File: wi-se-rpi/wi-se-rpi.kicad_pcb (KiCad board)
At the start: 4 copper layers, 29.2 x 19.5 mm, 43 parts, among them J1 RASPI, SW1 RESET, SW2 BOOT0, SW3 FLASH_EN_SW, U1 AMS1117-3.3, U2 ESP-WROOM-02, U3 MC74VHC1G, U4 NL27WZ00, U5 NL27WZ32

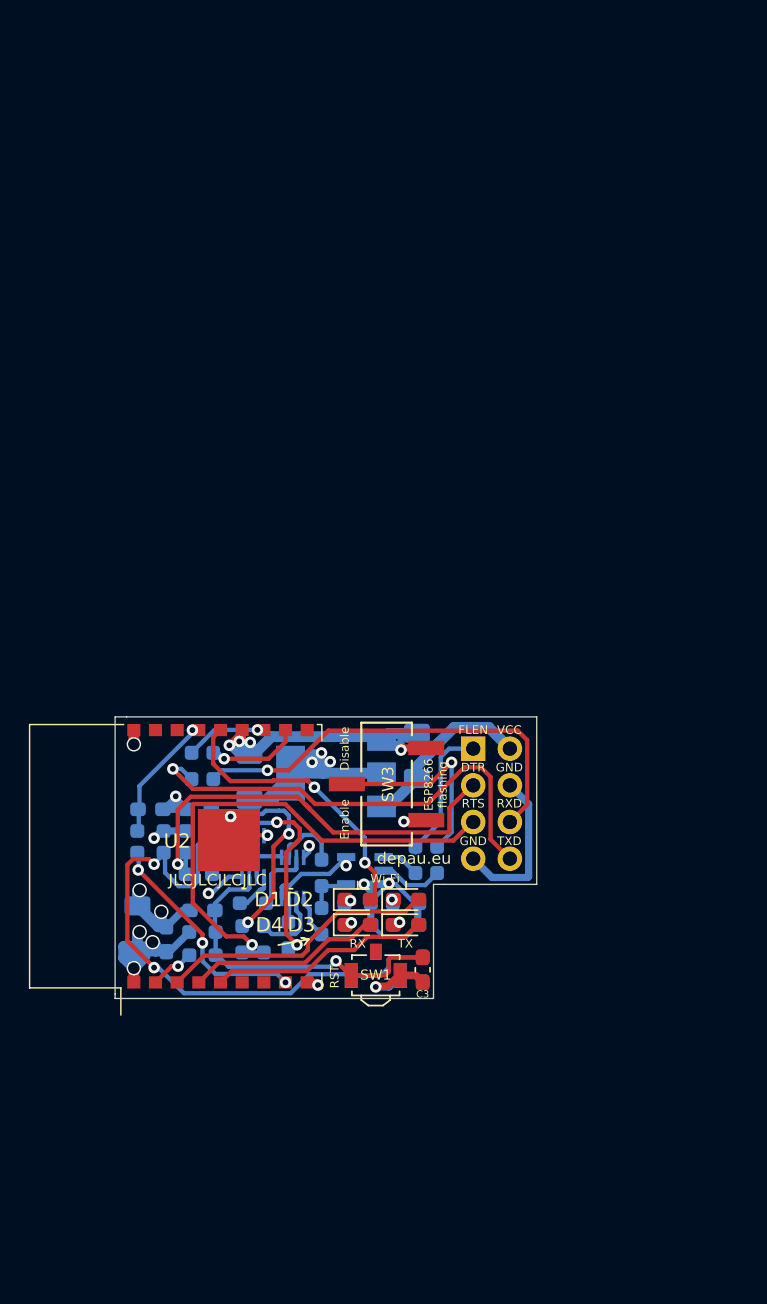
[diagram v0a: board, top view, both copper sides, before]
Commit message: Make RPI version as small as it can be
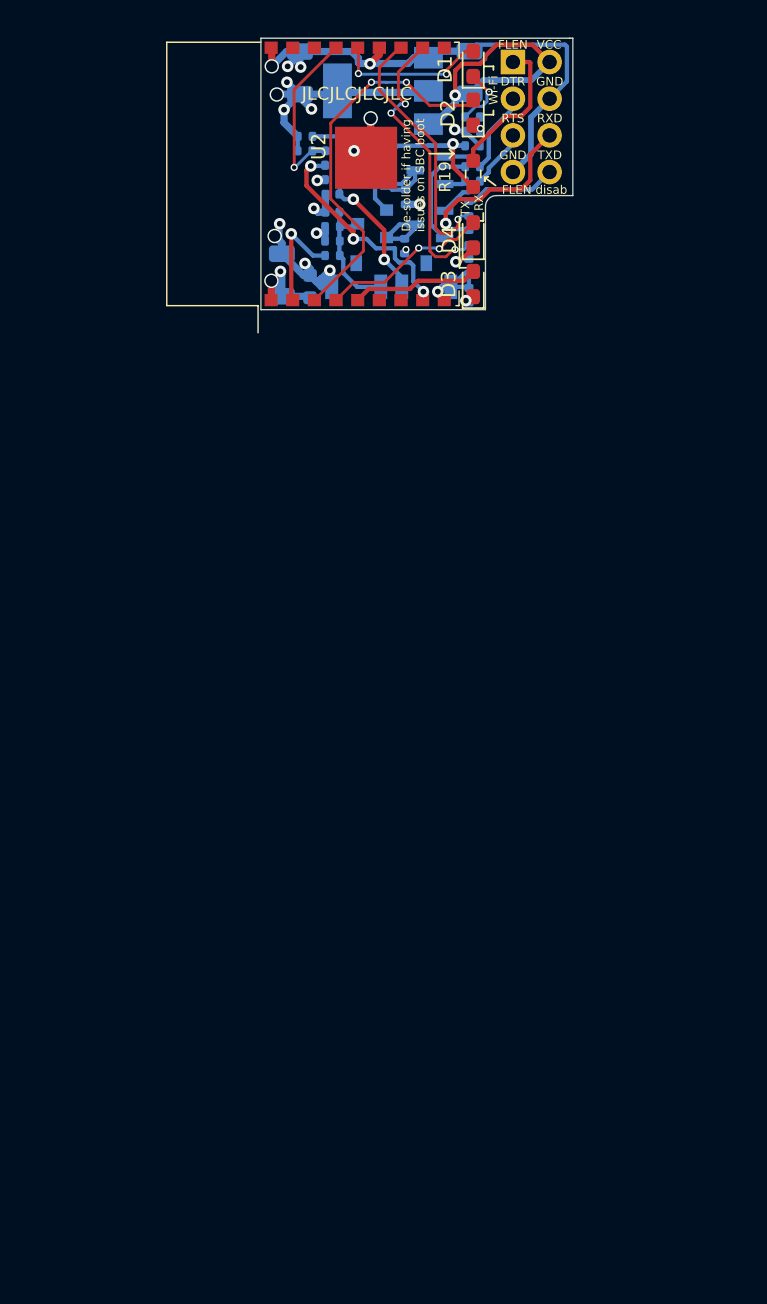
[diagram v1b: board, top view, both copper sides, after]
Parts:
- removed C3, C4: 0u1, Capacitor_SMD:C_0603_1608Metric_Pad1.08x0.95mm_HandSolder
- removed R20, R21: 10k, Resistor_SMD:R_0603_1608Metric_Pad0.98x0.95mm_HandSolder
- removed SW3: FLASH_EN_SW, JS102011SCQN:CK-JS102011SCQN-0-0-0
- removed U3: MC74VHC1G, ON-gates:SOT95P280X145-5N
- removed U4: NL27WZ00, ON-gates:SOP50P310X90-8N
- removed U5: NL27WZ32, ON-gates:SOP50P310X90-8N
- added Q1: SS8050-G, SS8050-G:SS8050-G, B.Cu at (85.0, 9.50)
- added Q2: SS8050-G, SS8050-G:SS8050-G, B.Cu at (85.0, 5.75)
- added Q3: 2N7002, Package_TO_SOT_SMD:SOT-23, B.Cu at (81.0, 9.45)
- added Q4: 2N7002, Package_TO_SOT_SMD:SOT-23, B.Cu at (81.0, 5.75)
- C1, C2, C5: footprint Capacitor_SMD:C_1206_3216Metric_Pad1.33x1.80mm_HandSolder -> Capacitor_SMD:C_1206_3216Metric
- C6: footprint Capacitor_SMD:C_0603_1608Metric_Pad1.08x0.95mm_HandSolder -> Capacitor_SMD:C_0603_1608Metric
- C7, C8, C9: footprint Capacitor_SMD:C_0603_1608Metric_Pad1.08x0.95mm_HandSolder -> Capacitor_SMD:C_0402_1005Metric
- R1, R14, R15, R16, R17, R18, R2, R3, R4, R5, R6, R7, R8, R9: footprint Resistor_SMD:R_0603_1608Metric_Pad0.98x0.95mm_HandSolder -> Resistor_SMD:R_0402_1005Metric
- R10, R11, R12, R13: value 0 -> 1k; footprint Resistor_SMD:R_0603_1608Metric_Pad0.98x0.95mm_HandSolder -> Resistor_SMD:R_0402_1005Metric
- R19: value 10k -> 0; moved to F.Cu
- SW1: footprint Button_Switch_SMD:SW_SPST_B3U-3100P -> wi-se:SW_SPST_B3U-3100P_silk_change; moved to B.Cu
- SW2: footprint Button_Switch_SMD:SW_SPST_B3U-3100P -> wi-se:SW_SPST_B3U-3100P_silk_change
- moved D1 58.4 mm to (88.0, -1.62), turned to 90 degrees
- moved R18 57.2 mm to (88.0, 4.05), turned to 180 degrees
- moved R1 55.0 mm to (88.0, 2.05)
- moved D2 54.7 mm to (88.0, 1.75), turned to 90 degrees
- moved R19 54.2 mm to (88.0, 6.00), turned to 270 degrees
- moved R2 53.6 mm to (88.0, 3.05), turned to 0 degrees
- moved R17 52.8 mm to (78.2, 6.40), turned to 180 degrees
- moved R10 49.3 mm to (78.2, 11.7)
- moved R13 49.2 mm to (78.2, 5.40)
- moved C8 49.2 mm to (78.2, 8.65)
- moved C2 48.9 mm to (76.0, -1.00)
- moved R6 48.7 mm to (78.2, 10.7)
- moved R5 48.7 mm to (76.4, 3.40)
- moved D4 48.4 mm to (88.0, 10.2), turned to 90 degrees
- moved R7 48.3 mm to (76.3, 4.40), turned to 0 degrees
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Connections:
- J1 pad 1: FLASH_EN -> Net-(J1-Pad1)
- R14 pad 2: DTR -> +3V3
- R15 pad 2: Net-(R15-Pad2) -> +3V3
- R16 pad 1: Net-(R16-Pad1) -> EN
- R16 pad 2: Net-(R15-Pad2) -> +3V3
- R17 pad 1: Net-(R17-Pad1) -> BOOT0
- R17 pad 2: RTS -> +3V3
- R18 pad 1: Net-(R18-Pad1) -> GND
- R18 pad 2: RTS -> FLASH_EN
- R19 pad 1: Net-(R19-Pad1) -> Net-(J1-Pad1)
- R19 pad 2: Net-(R19-Pad2) -> FLASH_EN
- R8 pad 2: FLASH_EN -> DTR
- R9 pad 1: Net-(R9-Pad1) -> RTS
- R9 pad 2: FLASH_EN_SW -> Net-(Q2-Pad2)
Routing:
- net RTS: track 35.1 -> 7.41 mm, vias 1 -> 0
- net BOOT0: track 45.9 -> 18.7 mm
- net TXD: track 32.1 -> 6.43 mm, vias 1 -> 0
- net DTR: track 30.6 -> 8.39 mm, vias 1 -> 0
- net +3V3: track 48.4 -> 28.3 mm
- net RXD: track 29.8 -> 13.4 mm
- net Net-(R19-Pad1): track 14.8 -> 0.00 mm, vias 2 -> 0
- net EN: track 23.4 -> 8.64 mm, vias 1 -> 0
- net Net-(R18-Pad1): track 14.5 -> 0.00 mm, vias 2 -> 0
- net FLASH_EN_SW: track 14.1 -> 0.00 mm, vias 1 -> 0
- net Net-(R11-Pad1): track 6.47 -> 19.9 mm, vias 1 -> 3
- net Net-(R12-Pad1): track 5.66 -> 18.2 mm
- net Net-(J1-Pad1): track 0.00 -> 10.3 mm
- net GND: track 77.9 -> 68.3 mm, vias 15 -> 13
- net LED_WIFI: track 19.9 -> 10.5 mm
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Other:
- board size 29.2 x 19.5 mm -> 21.6 x 18.8 mm
- rule via_min_drill: 0.3 -> 0.2
- rule via_min_size: 0.4 -> 0.45
- board text added: "De-solder if having issues on SBC boot"
- board text added: "FLEN disab"
- board text added: "IO0"
- board text added: "v0.1 for rpi"
- board text removed: "BOOT0"
- board text removed: "Disable"
- board text removed: "ESP8266 flashing"
- board text removed: "Enable"
- board text removed: "v0.1 for *pi"

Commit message: Final version of rpi variant (last famous words)
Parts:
- moved SW1 0.76 mm to (80.0, 13.8)
- moved SW2 0.72 mm to (84.8, 13.7)
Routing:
- net EN: track 8.64 -> 9.43 mm
- net Net-(D3-Pad1): track 0.89 -> 1.46 mm
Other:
- board size 21.6 x 18.8 mm -> 21.6 x 20 mm

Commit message: Ground switch shields
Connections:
- SW1 pad 3: (no net) -> GND
- SW2 pad 3: (no net) -> GND
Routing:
- net GND: track 68.3 -> 85.6 mm, vias 13 -> 16

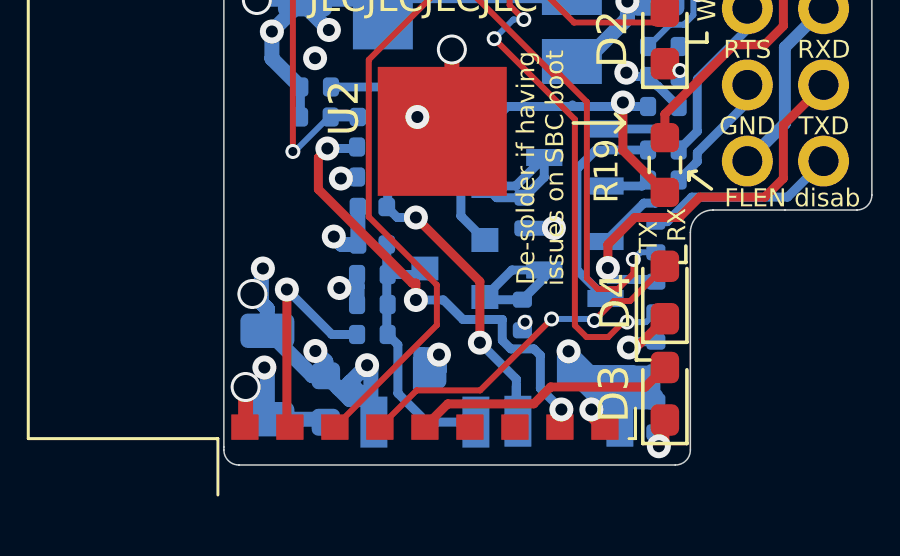
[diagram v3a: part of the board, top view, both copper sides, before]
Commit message: Replace buttons with cheap aliexpress ones
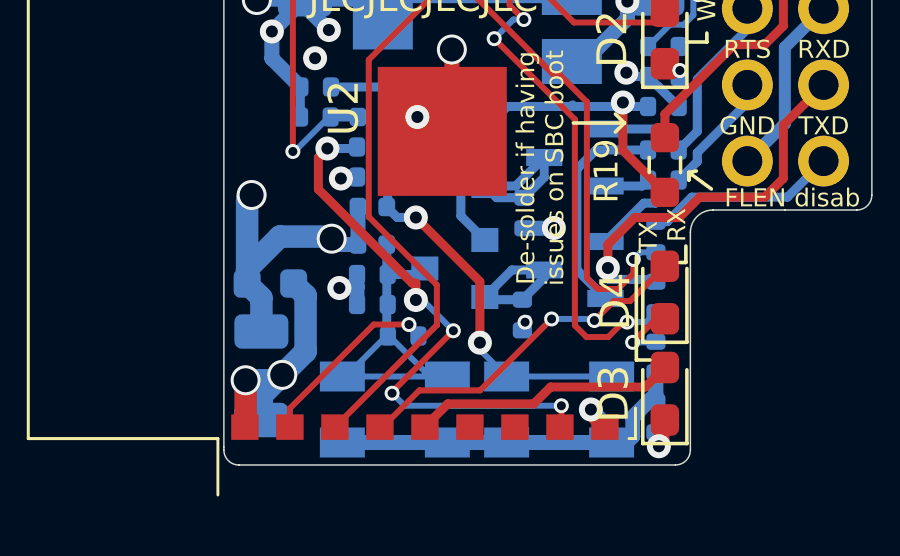
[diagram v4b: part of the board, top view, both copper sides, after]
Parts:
- C1, C2, C5: value 22u -> 10u
- SW1, SW2: footprint wi-se:SW_SPST_B3U-3100P_silk_change -> aliexpress-switch:Tactile_Push_Button_SMD_3x3x1.5mm.kicad_mod
- moved C6 4.27 mm to (74.8, 9.95), turned to 180 degrees
- moved SW1 1.08 mm to (79.0, 14.2)
- moved R10 1.03 mm to (79.3, 11.7), turned to 180 degrees
- moved SW2 0.54 mm to (84.5, 14.2), turned to 180 degrees
- moved C5 0.20 mm to (74.5, 13.0)
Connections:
- U2 pad 10: Net-(U2-Pad10) -> (no net)
- U2 pad 16: Net-(U2-Pad16) -> (no net)
- U2 pad 17: Net-(U2-Pad17) -> (no net)
- U2 pad 6: Net-(U2-Pad6) -> (no net)
- U2 pad 7: Net-(U2-Pad7) -> (no net)
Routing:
- net GND: track 85.6 -> 74.9 mm, vias 16 -> 11
- net +3V3: track 28.3 -> 31.5 mm
- net Net-(R13-Pad2): track 15.6 -> 18.8 mm, vias 3 -> 5
- net EN: track 9.43 -> 12.5 mm
- net BOOT0: track 18.7 -> 20.4 mm
- net Net-(R10-Pad1): track 7.59 -> 6.21 mm

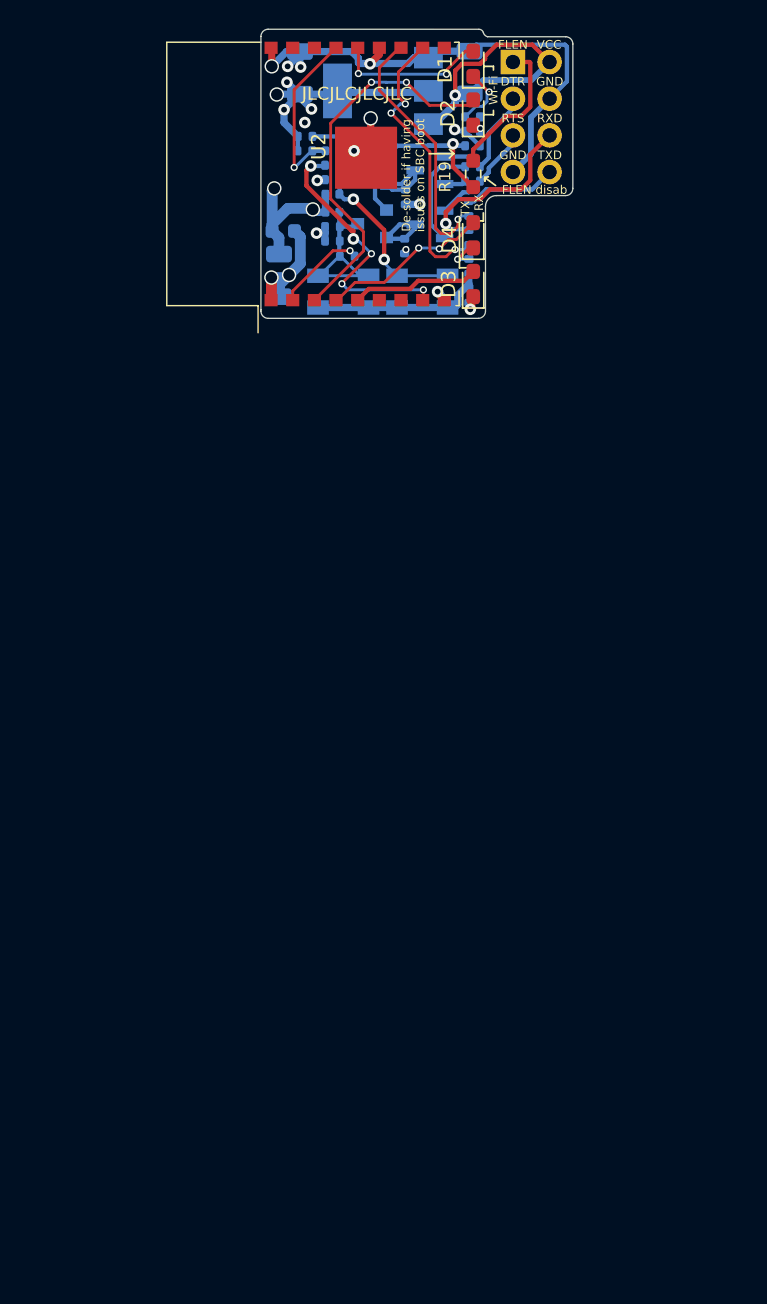
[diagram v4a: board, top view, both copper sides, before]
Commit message: rpi: Add missing GPIO15 pull-down
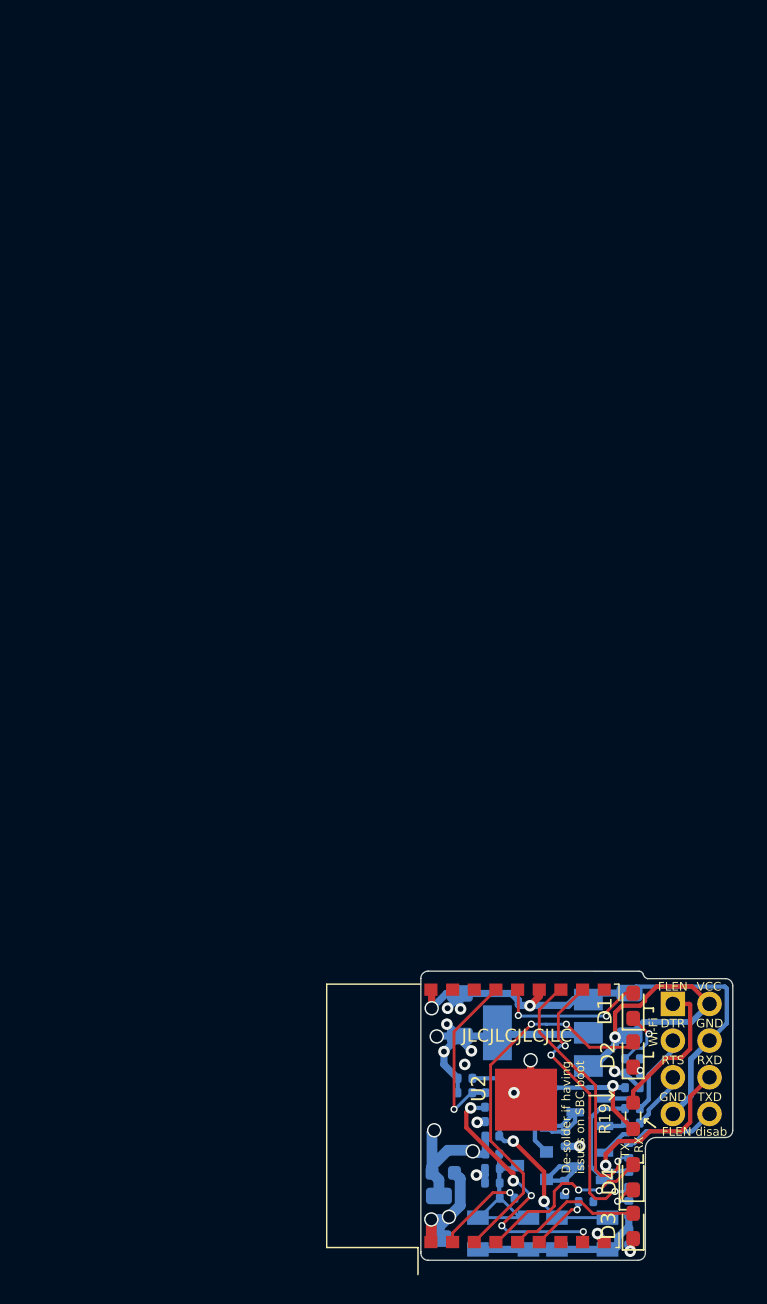
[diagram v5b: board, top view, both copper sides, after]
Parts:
- added R20: 10k, Resistor_SMD:R_0402_1005Metric, B.Cu at (95.8, 77.2)
- moved C1 66.2 mm to (98.8, 64.2)
- moved D1 66.2 mm to (99.1, 63.6)
- moved J1 66.2 mm to (101.8, 63.5)
- moved R15 66.2 mm to (94.4, 72.8)
- moved C2 66.2 mm to (87.1, 64.2)
- moved C5 66.2 mm to (85.6, 78.3)
- moved C6 66.2 mm to (85.9, 75.2)
- moved C7 66.2 mm to (89.3, 72.6)
- moved C8 66.2 mm to (89.3, 73.9)
- moved C9 66.2 mm to (89.3, 69.6)
- moved D2 66.2 mm to (99.1, 67.0)
- moved D3 66.2 mm to (99.1, 78.9)
- moved D4 66.2 mm to (99.1, 75.5)
- moved Q1 66.2 mm to (96.1, 74.7)
- moved Q2 66.2 mm to (96.1, 71.0)
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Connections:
- U2 pad 6: (no net) -> Net-(R20-Pad2)
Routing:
- net Net-(R20-Pad2): track 0.00 -> 4.15 mm, vias 0 -> 1
- net LED_RX: track 11.8 -> 12.7 mm
- net LED_TX: track 8.83 -> 9.49 mm
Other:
- outline, holes or cut-outs redrawn
- board text added: "v0.2 for rpi"
- board text removed: "v0.1 for rpi"
